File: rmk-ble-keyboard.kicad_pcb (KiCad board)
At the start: 2 copper layers, 285 x 94.5 mm, 172 parts, among them J1 USB_C_Receptacle_USB2.0_16P, J3 Debug, J4 RGB, J5 Reset, J6 JST-SM02B-SRSS-TB, Q1 Si2301CDS, SW1 esc, SW10 9, SW11 0, SW12 -, SW13 =, SW14 backspace, SW15 tab, SW16 q, SW17 w, SW18 e, SW19 r, SW2 1, SW20 t, SW21 y, SW22 u, SW23 i, SW24 o, SW25 p, SW26 [, SW27 ], SW28 \, SW29 capslock, SW3 2, SW30 a, SW31 s, SW32 d, SW33 f, SW34 g, SW35 h, SW36 j, SW37 k, SW38 l, SW39 ;, SW4 3, SW40 ', SW41 enter, SW42 lshift, SW43 z, SW44 x, SW45 c, SW46 v, SW47 b, SW48 n, SW49 m, SW5 4, SW50 ,, SW51 ., SW52 /, SW53 rshift, SW54 lctrl, SW55 lgui, SW56 lalt, SW57 space, SW58 ralt, SW59 rgui, SW6 5, SW60 fn, SW61 rctrl, SW62 MSK-12C02, SW7 6, SW8 7, SW9 8, U2 USBLC6-2SC6, U3 TP4056, U5 AP2112K-3.3, Y1 32.768KHZ

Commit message: update production pcb version
Signed-off-by: HaoboGu <haobogu@outlook.com>
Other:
- board text added: "Li+"
- board text added: "Li-"
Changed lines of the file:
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@@
 		(layer "Edge.Cuts")
+	)
+	(gr_text "Li+"
+		(at 136.39 79.64 0)
+		(layer "B.SilkS")
+		(effects
+			(font
+				(size 1.5 1.5)
+				(thickness 0.3)
+				(bold yes)
+			)
+			(justify left bottom mirror)
+		)
+	)
+	(gr_text "Li-"
+		(at 143.9 79.88 0)
+		(layer "B.SilkS")
+		(effects
+			(font
+				(size 1.5 1.5)
+				(thickness 0.3)
+				(bold yes)
+			)
+			(justify left bottom mirror)
+		)
 	)
 	(gr_text "Firmware at: github.com/haobogu/rmk"

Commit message: update footprints
Signed-off-by: HaoboGu <haobogu@outlook.com>
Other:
- board text added: "5v"
- board text added: "Reset"
- board text added: "gnd"
- board text added: "off"
- board text added: "on"
- board text added: "rgb"
- board text added: "swc"
- board text added: "swd"
- board text added: "vcc"

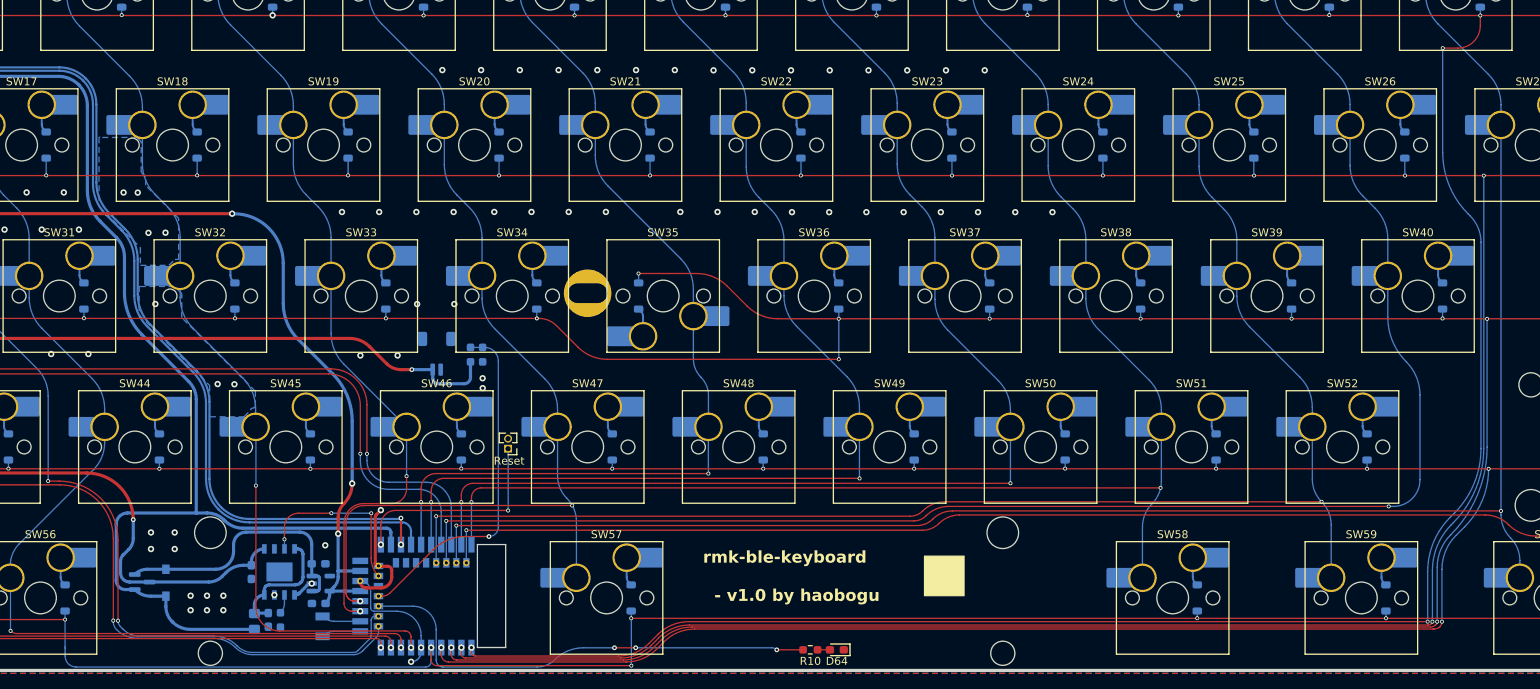
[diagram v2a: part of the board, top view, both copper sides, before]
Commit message: feat: add firmware, update readme, fix FATAL error
Signed-off-by: HaoboGu <haobogu@outlook.com>
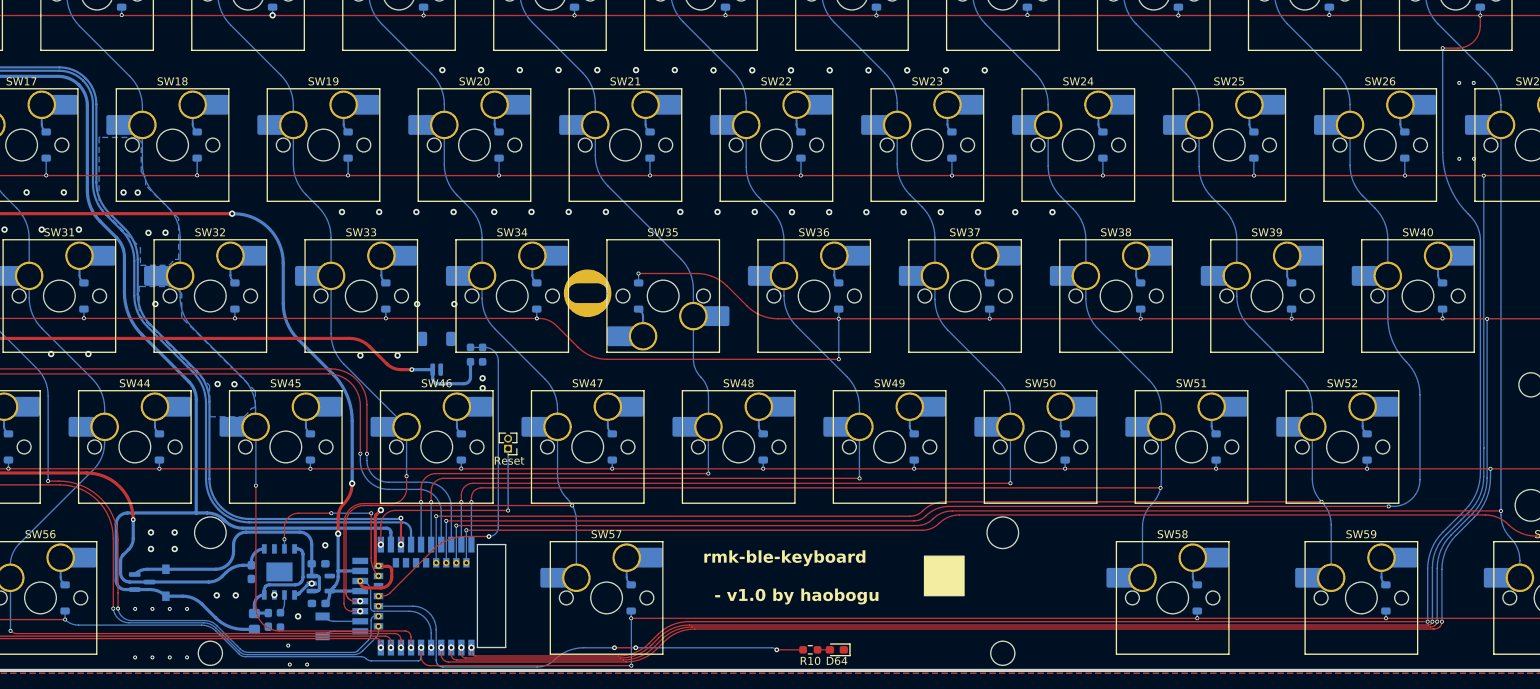
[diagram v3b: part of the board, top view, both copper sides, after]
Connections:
- U1 pad 5: /matrix/row5 -> GND
- U1 pad 6: GND -> /matrix/row5
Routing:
- net /matrix/row5: track 285.1 -> 280.8 mm
- net VBUS: track 209.9 -> 208.4 mm
- net /mcu/caps: track 129.2 -> 128.4 mm
- net /mcu/rgb: track 137.5 -> 136.8 mm
- net /matrix/row2: track 468.1 -> 468.7 mm
- net GND: track 34.1 -> 33.6 mm, vias 98 -> 109
